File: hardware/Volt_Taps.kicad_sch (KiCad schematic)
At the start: 16 parts

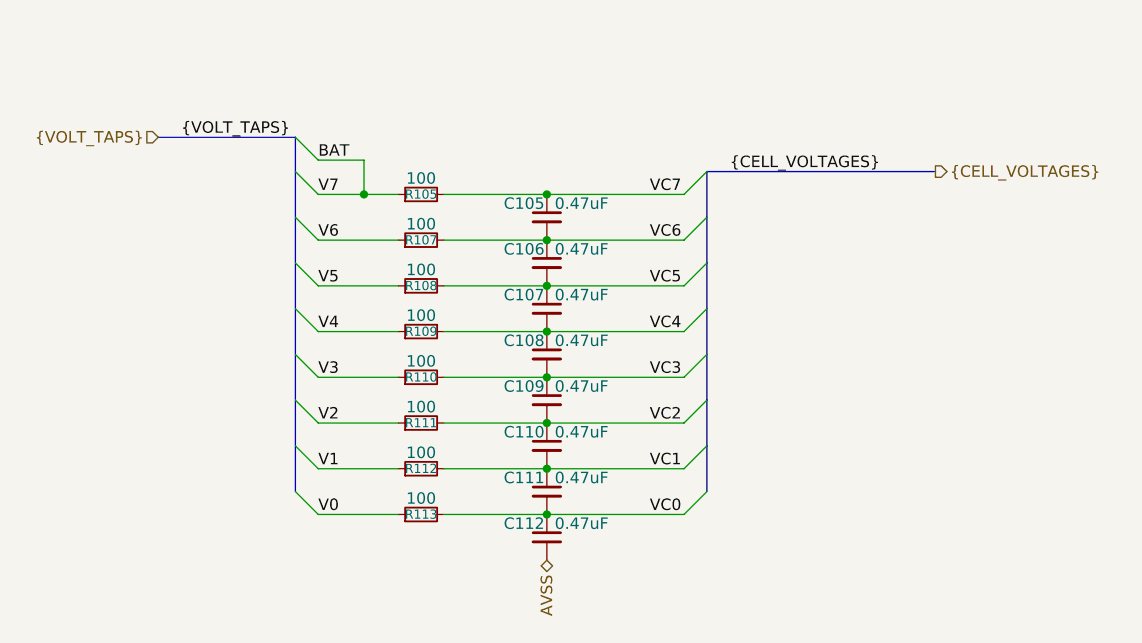
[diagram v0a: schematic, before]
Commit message: updated sheets, footprint, and calcs; 2nd review changes
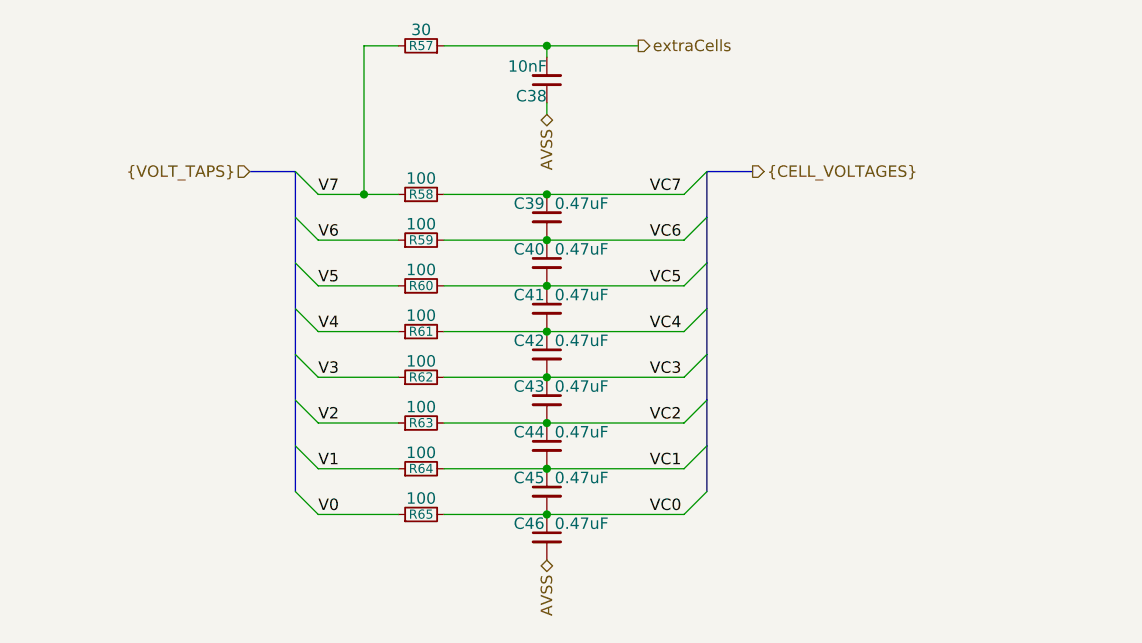
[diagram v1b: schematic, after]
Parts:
- added C38: 10nF, Capacitor_SMD:C_0805_2012Metric_Pad1.18x1.45mm_HandSolder, symbol Device:C_Small
- added R57: 30, Resistor_SMD:R_0603_1608Metric_Pad0.98x0.95mm_HandSolder, symbol Device:R_Small
- C39: renamed from C105; footprint (none) -> Capacitor_SMD:C_0603_1608Metric_Pad1.08x0.95mm_HandSolder
- C40: renamed from C106; footprint (none) -> Capacitor_SMD:C_0603_1608Metric_Pad1.08x0.95mm_HandSolder
- C41: renamed from C107; footprint (none) -> Capacitor_SMD:C_0603_1608Metric_Pad1.08x0.95mm_HandSolder
- C42: renamed from C108; footprint (none) -> Capacitor_SMD:C_0603_1608Metric_Pad1.08x0.95mm_HandSolder
- C43: renamed from C109; footprint (none) -> Capacitor_SMD:C_0603_1608Metric_Pad1.08x0.95mm_HandSolder
- C44: renamed from C110; footprint (none) -> Capacitor_SMD:C_0603_1608Metric_Pad1.08x0.95mm_HandSolder
- C45: renamed from C111; footprint (none) -> Capacitor_SMD:C_0603_1608Metric_Pad1.08x0.95mm_HandSolder
- C46: renamed from C112; footprint (none) -> Capacitor_SMD:C_0603_1608Metric_Pad1.08x0.95mm_HandSolder
- R58: renamed from R105; footprint (none) -> Resistor_SMD:R_0805_2012Metric_Pad1.20x1.40mm_HandSolder
- R59: renamed from R107; footprint (none) -> Resistor_SMD:R_0805_2012Metric_Pad1.20x1.40mm_HandSolder
- R60: renamed from R108; footprint (none) -> Resistor_SMD:R_0805_2012Metric_Pad1.20x1.40mm_HandSolder
- R61: renamed from R109; footprint (none) -> Resistor_SMD:R_0805_2012Metric_Pad1.20x1.40mm_HandSolder
- R62: renamed from R110; footprint (none) -> Resistor_SMD:R_0805_2012Metric_Pad1.20x1.40mm_HandSolder
- R63: renamed from R111; footprint (none) -> Resistor_SMD:R_0805_2012Metric_Pad1.20x1.40mm_HandSolder
- R64: renamed from R112; footprint (none) -> Resistor_SMD:R_0805_2012Metric_Pad1.20x1.40mm_HandSolder
- R65: renamed from R113; footprint (none) -> Resistor_SMD:R_0805_2012Metric_Pad1.20x1.40mm_HandSolder
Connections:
- net AVSS: now also C38.1
- net BAT renamed V7
- net V7: now also R57.2
- new net extraCells: C38.2, R57.1
